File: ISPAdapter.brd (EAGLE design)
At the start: 63 x 34 mm, 3 parts

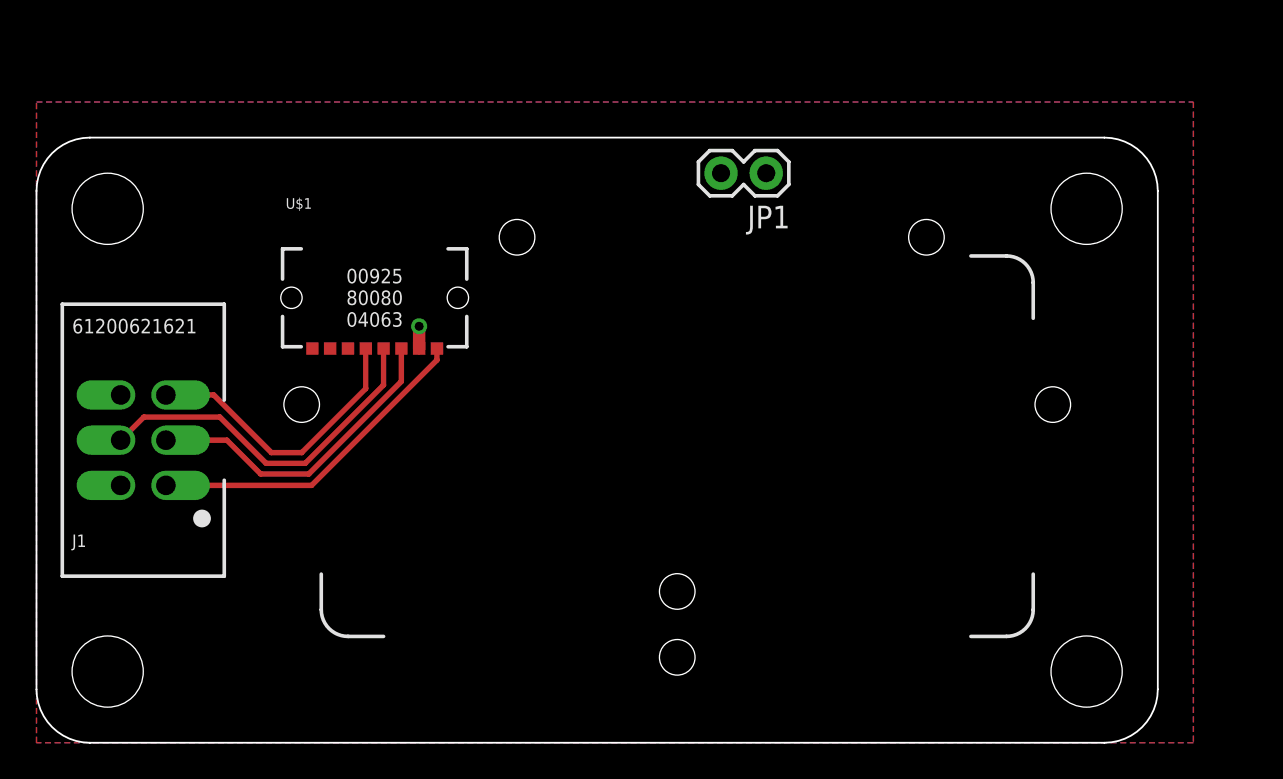
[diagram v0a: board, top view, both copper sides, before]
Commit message: Dropped ground layer
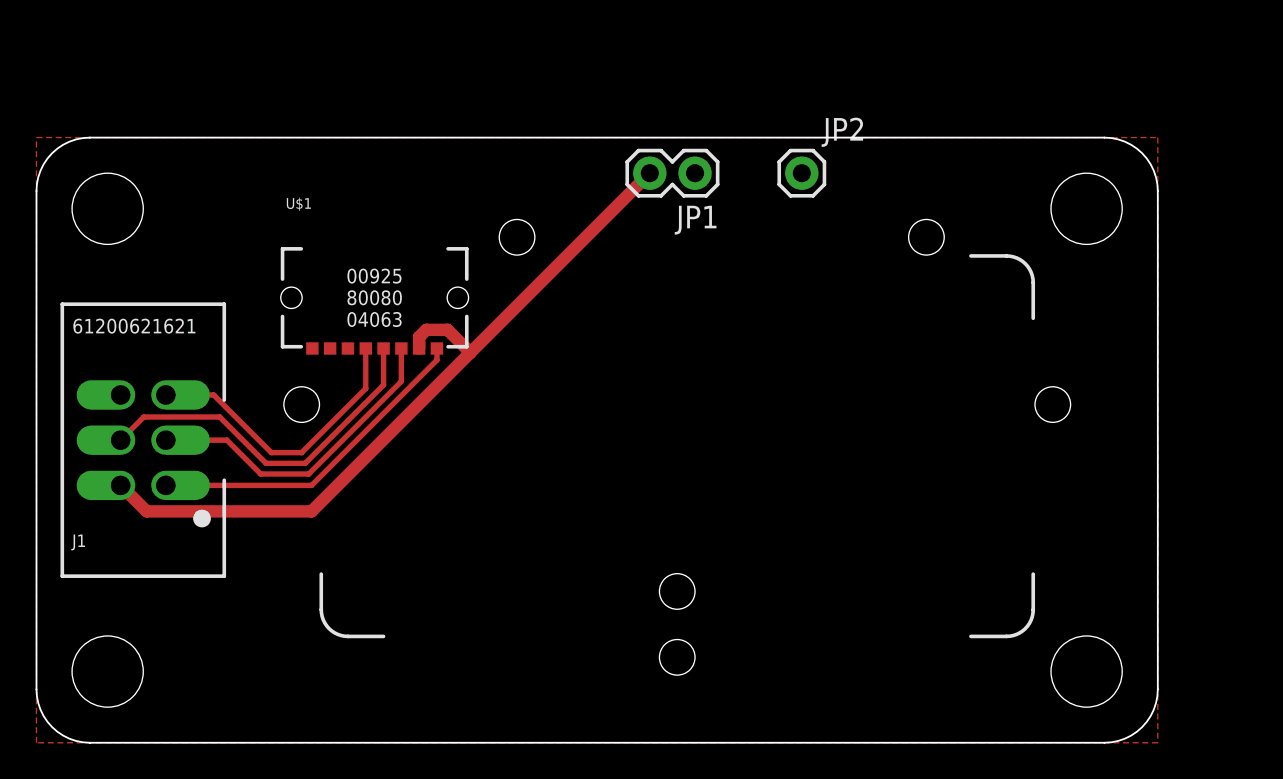
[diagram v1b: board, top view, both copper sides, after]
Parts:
- added JP2: M01PTH, SparkFun-Connectors:1X01
- moved JP1 4.00 mm to (37.0, 32.0)
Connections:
- net GND: now also JP2.1
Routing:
- net VCC: track 1.25 -> 42.4 mm, vias 1 -> 0
- removed copper zone on layer 16, net VCC
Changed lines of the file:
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@@
 <layer number="14" name="Route14" color="1" fill="6" visible="no" active="no"/>
 <layer number="15" name="Route15" color="4" fill="6" visible="no" active="no"/>
-<layer number="16" name="Bottom" color="1" fill="1" visible="no" active="yes"/>
+<layer number="16" name="Bottom" color="1" fill="1" visible="yes" active="yes"/>
 <layer number="17" name="Pads" color="2" fill="1" visible="yes" active="yes"/>
 <layer number="18" name="Vias" color="2" fill="1" visible="yes" active="yes"/>
@@
 <hole x="57.1" y="19" drill="2"/>
 <hole x="14.9" y="19" drill="2"/>
-<text x="41" y="30.2" size="1" layer="107" font="vector" ratio="20" rot="SR270" align="center-left">GND</text>
+<text x="37" y="30.2" size="1" layer="107" font="vector" ratio="20" rot="SR270" align="center-left">GND</text>
 <circle x="4" y="30" radius="2.7" width="0.5" layer="107"/>
-<text x="38.5" y="30.2" size="1" layer="107" font="vector" ratio="20" rot="SR270" align="center-left">+5V</text>
+<text x="34.5" y="30.2" size="1" layer="107" font="vector" ratio="20" rot="SR270" align="center-left">+5V</text>
 <text x="26" y="9" size="1" layer="107" font="vector" ratio="20" rot="SR0">1 MISO</text>
 <text x="19" y="9" size="1" layer="107" font="vector" ratio="20" rot="SR0">2 VCC</text>
@@
 <circle x="36" y="4.8" radius="1.7" width="0.5" layer="107"/>
 <circle x="14.9" y="19" radius="1.7" width="0.5" layer="107"/>
+<text x="43" y="30.2" size="1" layer="107" font="vector" ratio="20" rot="SR270" align="center-left">GND</text>
 </plain>
 <attributes>
@@
 <attribute name="DIGIKEY_PART_#" value="732-5394-ND" x="6" y="17" size="1.778" layer="27" display="off"/>
 </element>
-<element name="JP1" library="SparkFun-Connectors" package="1X02" value="M02PTH" x="41" y="32" rot="R180"/>
+<element name="JP1" library="SparkFun-Connectors" package="1X02" value="M02PTH" x="37" y="32" rot="R180"/>
 <element name="U$1" library="dubec" package="AVX9258-8P" value="AVX9258" x="19" y="25">
 <attribute name="MANUFACTURER" value="AVX Corporation" x="19" y="25" size="1.778" layer="27" display="off"/>
@@
 <attribute name="DIGIKEY_PART_#" value="478-5495-1-ND" x="19" y="25" size="1.778" layer="27" display="off"/>
 </element>
+<element name="JP2" library="SparkFun-Connectors" package="1X01" value="M01PTH" x="43" y="32"/>
 </elements>
 <signals>
@@
 <contactref element="JP1" pad="2"/>
 <contactref element="U$1" pad="2"/>
-<polygon width="0.3048" layer="16">
-<vertex x="0" y="0"/>
-<vertex x="0" y="36"/>
-<vertex x="65" y="36"/>
-<vertex x="65" y="0"/>
-</polygon>
-<via x="21.5" y="23.4" extent="1-16" drill="0.5"/>
-<wire x1="21.5" y1="22.15" x2="21.5" y2="23.4" width="0.7" layer="1"/>
+<wire x1="34.46" y1="32" x2="24.38" y2="21.92" width="0.7" layer="1"/>
+<wire x1="24.38" y1="21.92" x2="15.46" y2="13" width="0.7" layer="1"/>
+<wire x1="15.46" y1="13" x2="6.19" y2="13" width="0.7" layer="1"/>
+<wire x1="6.19" y1="13" x2="4.73" y2="14.46" width="0.7" layer="1"/>
+<wire x1="21.5" y1="22.15" x2="21.5" y2="22.8" width="0.7" layer="1"/>
+<wire x1="21.5" y1="22.8" x2="21.9" y2="23.2" width="0.7" layer="1"/>
+<wire x1="21.9" y1="23.2" x2="23.1" y2="23.2" width="0.7" layer="1"/>
+<wire x1="23.1" y1="23.2" x2="24.38" y2="21.92" width="0.7" layer="1"/>
 </signal>
 <signal name="MOSI">
@@
 <polygon width="0.3556" layer="1">
 <vertex x="0" y="0"/>
-<vertex x="0" y="36"/>
-<vertex x="65" y="36"/>
-<vertex x="65" y="0"/>
+<vertex x="0" y="34"/>
+<vertex x="63" y="34"/>
+<vertex x="63" y="0"/>
 </polygon>
 <contactref element="U$1" pad="8"/>
 <contactref element="U$1" pad="7"/>
 <contactref element="U$1" pad="6"/>
+<contactref element="JP2" pad="1"/>
 </signal>
 <signal name="MISO">

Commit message: Grounded screw holes; disconnected unused connector pins
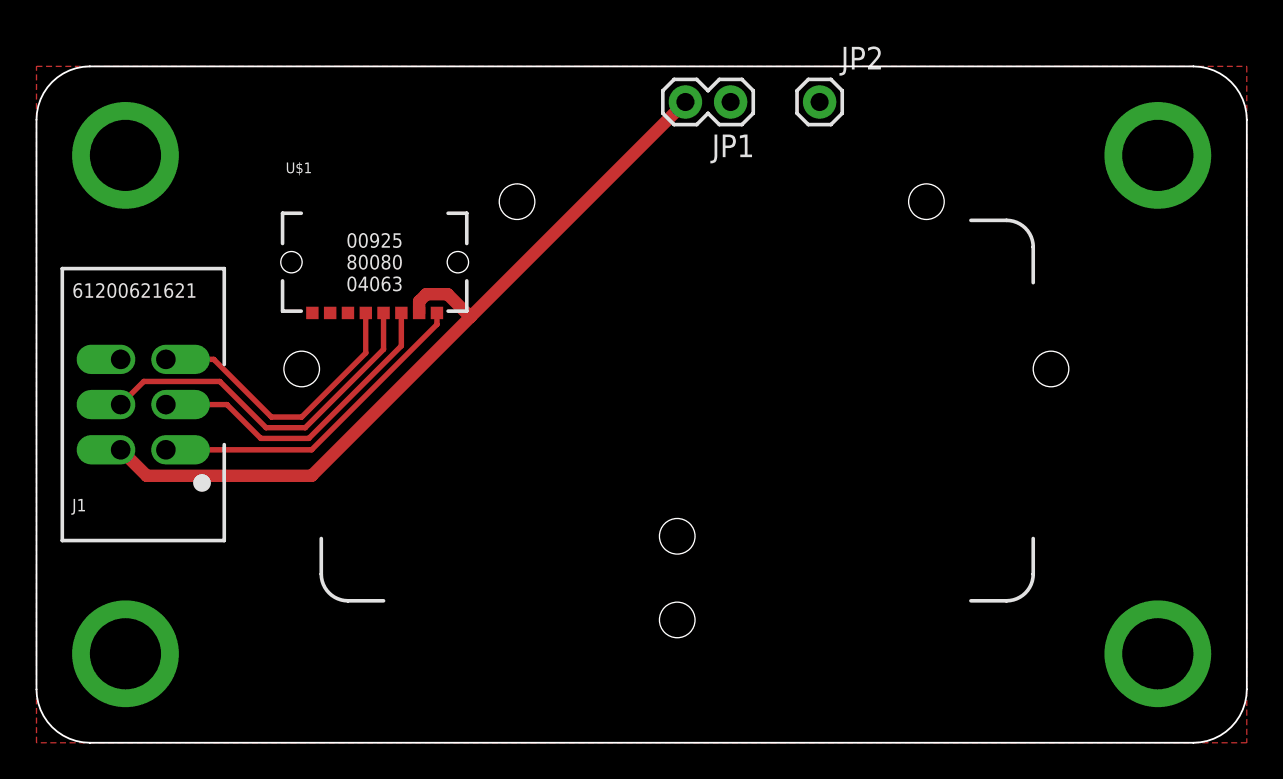
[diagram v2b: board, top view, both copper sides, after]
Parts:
- moved JP1 4.47 mm to (39.0, 36.0)
- moved JP2 4.12 mm to (44.0, 36.0)
- moved J1 2.00 mm to (6.00, 19.0)
- moved U$1 2.00 mm to (19.0, 27.0)
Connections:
- net GND: no longer U$1.7, U$1.8
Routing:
- net VCC: track 42.4 -> 45.3 mm
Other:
- board size 63 x 34 mm -> 68 x 38 mm

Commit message: Kelvin join?
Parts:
- moved JP2 9.70 mm to (34.3, 36.0)
- moved JP1 2.70 mm to (41.7, 36.0), turned to 0 degrees
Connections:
- new net DGND: J1.6, JP1.1, U$1.6
- net GND: no longer J1.6, JP1.1, U$1.6
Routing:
- net DGND: track 0.00 -> 44.0 mm
- net VCC: track 45.3 -> 53.0 mm
- net GND: track 0.00 -> 1.41 mm
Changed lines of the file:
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@@
 <hole x="57" y="21" drill="2"/>
 <hole x="14.9" y="21" drill="2"/>
-<text x="39.1" y="34.2" size="1" layer="107" font="vector" ratio="20" rot="SR270" align="center-left">GND</text>
-<text x="36.5" y="34.2" size="1" layer="107" font="vector" ratio="20" rot="SR270" align="center-left">+5V</text>
+<text x="41.7" y="34" size="1" layer="107" font="vector" ratio="20" rot="SR270" align="center-left">GND</text>
+<text x="44.3" y="34" size="1" layer="107" font="vector" ratio="20" rot="SR270" align="center-left">+5V</text>
 <text x="26" y="11" size="1" layer="107" font="vector" ratio="20" rot="SR0">1 MISO</text>
 <text x="19" y="11" size="1" layer="107" font="vector" ratio="20" rot="SR0">2 VCC</text>
@@
 <circle x="36" y="6.9" radius="1.7" width="0.5" layer="107"/>
 <circle x="14.9" y="21" radius="1.7" width="0.5" layer="107"/>
-<text x="44.1" y="34.2" size="1" layer="107" font="vector" ratio="20" rot="SR270" align="center-left">GND</text>
+<text x="34.3" y="34" size="1" layer="107" font="vector" ratio="20" rot="SR270" align="center-left">GND</text>
 </plain>
 <attributes>
@@
 <attribute name="DIGIKEY_PART_#" value="732-5394-ND" x="6" y="19" size="1.778" layer="27" display="off"/>
 </element>
-<element name="JP1" library="SparkFun-Connectors" package="1X02" value="M02PTH" x="39" y="36" rot="R180"/>
+<element name="JP1" library="SparkFun-Connectors" package="1X02" value="M02PTH" x="41.7" y="36"/>
 <element name="U$1" library="dubec" package="AVX9258-8P" value="AVX9258" x="19" y="27">
 <attribute name="MANUFACTURER" value="AVX Corporation" x="19" y="27" size="1.778" layer="27" display="off"/>
@@
 <attribute name="DIGIKEY_PART_#" value="478-5495-1-ND" x="19" y="27" size="1.778" layer="27" display="off"/>
 </element>
-<element name="JP2" library="SparkFun-Connectors" package="1X01" value="M01PTH" x="44" y="36"/>
+<element name="JP2" library="SparkFun-Connectors" package="1X01" value="M01PTH" x="34.3" y="36"/>
 </elements>
 <signals>
@@
 <contactref element="JP1" pad="2"/>
 <contactref element="U$1" pad="2"/>
-<wire x1="36.46" y1="36" x2="24.38" y2="23.92" width="0.7" layer="1"/>
+<wire x1="44.24" y1="36" x2="32.16" y2="23.92" width="0.7" layer="1"/>
 <wire x1="24.38" y1="23.92" x2="15.46" y2="15" width="0.7" layer="1"/>
 <wire x1="15.46" y1="15" x2="6.19" y2="15" width="0.7" layer="1"/>
@@
 <wire x1="21.9" y1="25.2" x2="23.1" y2="25.2" width="0.7" layer="1"/>
 <wire x1="23.1" y1="25.2" x2="24.38" y2="23.92" width="0.7" layer="1"/>
+<wire x1="32.16" y1="23.92" x2="24.38" y2="23.92" width="0.7" layer="1"/>
 </signal>
 <signal name="MOSI">
@@
 <wire x1="6.03" y1="20.3" x2="4.73" y2="19" width="0.3048" layer="1"/>
 </signal>
-<signal name="GND">
+<signal name="DGND">
 <contactref element="J1" pad="6"/>
 <contactref element="JP1" pad="1"/>
-<polygon width="0.3556" layer="1">
-<vertex x="0" y="0"/>
-<vertex x="0" y="38"/>
-<vertex x="68" y="38"/>
-<vertex x="68" y="0"/>
-</polygon>
-<contactref element="JP2" pad="1"/>
 <contactref element="U$1" pad="6"/>
-<via x="5" y="33" extent="1-16" drill="4"/>
-<via x="5" y="5" extent="1-16" drill="4"/>
-<via x="63" y="5" extent="1-16" drill="4"/>
-<via x="63" y="33" extent="1-16" drill="4"/>
+<wire x1="41.7" y1="36" x2="34.2" y2="28.5" width="0.7" layer="1"/>
+<wire x1="34.2" y1="28.5" x2="20.9" y2="28.5" width="0.7" layer="1"/>
+<wire x1="20.9" y1="28.5" x2="17.5" y2="25.1" width="0.7" layer="1"/>
+<wire x1="17.5" y1="25.1" x2="17.5" y2="24.15" width="0.7" layer="1"/>
+<wire x1="4.73" y1="21.54" x2="6.19" y2="23" width="0.7" layer="1"/>
+<wire x1="6.19" y1="23" x2="17.1" y2="23" width="0.7" layer="1"/>
+<wire x1="17.1" y1="23" x2="17.5" y2="23.4" width="0.7" layer="1"/>
+<wire x1="17.5" y1="23.4" x2="17.5" y2="24.15" width="0.7" layer="1"/>
 </signal>
 <signal name="MISO">
@@
 <wire x1="9.96" y1="21.54" x2="7.27" y2="21.54" width="0.3048" layer="1"/>
 </signal>
+<signal name="GND">
+<polygon width="0.3556" layer="1">
+<vertex x="0" y="0"/>
+<vertex x="0" y="38"/>
+<vertex x="68" y="38"/>
+<vertex x="68" y="0"/>
+</polygon>
+<via x="4" y="34" extent="1-16" drill="3.1"/>
+<via x="4" y="4" extent="1-16" drill="3.1"/>
+<via x="64" y="34" extent="1-16" drill="3.1"/>
+<via x="64" y="4" extent="1-16" drill="3.1"/>
+<contactref element="JP2" pad="1"/>
+<wire x1="40.7" y1="37" x2="41.7" y2="36" width="0.3048" layer="1"/>
+</signal>
 </signals>
+<errors>
+</errors>
 </board>
 </drawing>

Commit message: Tidying
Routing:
- net RESET: track 16.3 -> 15.4 mm
- net SCK: track 18.0 -> 17.1 mm
- net MOSI: track 20.3 -> 19.3 mm
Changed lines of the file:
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@@
 <hole x="50" y="30.4" drill="2"/>
 <hole x="57" y="21" drill="2"/>
-<hole x="14.9" y="21" drill="2"/>
+<hole x="15" y="21" drill="2"/>
 <text x="41.7" y="34" size="1" layer="107" font="vector" ratio="20" rot="SR270" align="center-left">GND</text>
 <text x="44.3" y="34" size="1" layer="107" font="vector" ratio="20" rot="SR270" align="center-left">+5V</text>
@@
 for Super DUBEC.
 Rev. 1</text>
-<text x="10" y="3" size="1" layer="107" font="vector" ratio="20" align="top-left">http://TURBOFUNCTION.com/fpv</text>
+<text x="4" y="3.5" size="1" layer="107" font="vector" ratio="20" align="top-left">http://TURBOFUNCTION.com/fpv</text>
 <text x="18" y="18" size="1" layer="107" font="vector" ratio="20">ISP connector pins:</text>
 <hole x="36" y="6.9" drill="2"/>
@@
 <circle x="36" y="11.6" radius="1.7" width="0.5" layer="107"/>
 <circle x="36" y="6.9" radius="1.7" width="0.5" layer="107"/>
-<circle x="14.9" y="21" radius="1.7" width="0.5" layer="107"/>
+<circle x="15" y="21" radius="1.7" width="0.5" layer="107"/>
 <text x="34.3" y="34" size="1" layer="107" font="vector" ratio="20" rot="SR270" align="center-left">GND</text>
 </plain>
@@
 <contactref element="JP1" pad="2"/>
 <contactref element="U$1" pad="2"/>
-<wire x1="44.24" y1="36" x2="32.16" y2="23.92" width="0.7" layer="1"/>
-<wire x1="24.38" y1="23.92" x2="15.46" y2="15" width="0.7" layer="1"/>
-<wire x1="15.46" y1="15" x2="6.19" y2="15" width="0.7" layer="1"/>
+<wire x1="44.24" y1="36" x2="35.66" y2="27.42" width="0.7" layer="1"/>
+<wire x1="16.76" y1="16.7" x2="11.3" y2="16.7" width="0.7" layer="1"/>
+<wire x1="11.3" y1="16.7" x2="9.6" y2="15" width="0.7" layer="1"/>
+<wire x1="9.6" y1="15" x2="6.19" y2="15" width="0.7" layer="1"/>
 <wire x1="6.19" y1="15" x2="4.73" y2="16.46" width="0.7" layer="1"/>
 <wire x1="21.5" y1="24.15" x2="21.5" y2="24.8" width="0.7" layer="1"/>
-<wire x1="21.5" y1="24.8" x2="21.9" y2="25.2" width="0.7" layer="1"/>
-<wire x1="21.9" y1="25.2" x2="23.1" y2="25.2" width="0.7" layer="1"/>
-<wire x1="23.1" y1="25.2" x2="24.38" y2="23.92" width="0.7" layer="1"/>
-<wire x1="32.16" y1="23.92" x2="24.38" y2="23.92" width="0.7" layer="1"/>
+<wire x1="35.66" y1="27.42" x2="26.22" y2="27.42" width="0.7" layer="1"/>
+<wire x1="16.76" y1="16.7" x2="24" y2="23.94" width="0.7" layer="1"/>
+<wire x1="26.22" y1="27.42" x2="24" y2="25.2" width="0.7" layer="1"/>
+<wire x1="24" y1="25.2" x2="21.9" y2="25.2" width="0.7" layer="1"/>
+<wire x1="21.9" y1="25.2" x2="21.5" y2="24.8" width="0.7" layer="1"/>
+<wire x1="24" y1="23.94" x2="24" y2="25.2" width="0.7" layer="1"/>
 </signal>
 <signal name="MOSI">
 <contactref element="J1" pad="4"/>
 <contactref element="U$1" pad="4"/>
-<wire x1="19.5" y1="24.15" x2="19.5" y2="22.1" width="0.3048" layer="1"/>
-<wire x1="19.5" y1="22.1" x2="15.1" y2="17.7" width="0.3048" layer="1"/>
-<wire x1="15.1" y1="17.7" x2="12.9" y2="17.7" width="0.3048" layer="1"/>
-<wire x1="12.9" y1="17.7" x2="10.3" y2="20.3" width="0.3048" layer="1"/>
-<wire x1="10.3" y1="20.3" x2="6.03" y2="20.3" width="0.3048" layer="1"/>
+<wire x1="19.5" y1="24.15" x2="19.5" y2="22.3" width="0.3048" layer="1"/>
+<wire x1="19.5" y1="22.3" x2="15.9" y2="18.7" width="0.3048" layer="1"/>
+<wire x1="15.9" y1="18.7" x2="11.1" y2="18.7" width="0.3048" layer="1"/>
+<wire x1="11.1" y1="18.7" x2="9.5" y2="20.3" width="0.3048" layer="1"/>
+<wire x1="9.5" y1="20.3" x2="6.03" y2="20.3" width="0.3048" layer="1"/>
 <wire x1="6.03" y1="20.3" x2="4.73" y2="19" width="0.3048" layer="1"/>
 </signal>
@@
 <contactref element="JP1" pad="1"/>
 <contactref element="U$1" pad="6"/>
-<wire x1="41.7" y1="36" x2="34.2" y2="28.5" width="0.7" layer="1"/>
-<wire x1="34.2" y1="28.5" x2="20.9" y2="28.5" width="0.7" layer="1"/>
-<wire x1="20.9" y1="28.5" x2="17.5" y2="25.1" width="0.7" layer="1"/>
-<wire x1="17.5" y1="25.1" x2="17.5" y2="24.15" width="0.7" layer="1"/>
+<wire x1="35.3" y1="28.5" x2="23.1" y2="28.5" width="0.7" layer="1"/>
+<wire x1="23.1" y1="28.5" x2="19.8" y2="25.2" width="0.7" layer="1"/>
+<wire x1="19.8" y1="25.2" x2="17.9" y2="25.2" width="0.7" layer="1"/>
+<wire x1="17.9" y1="25.2" x2="17.5" y2="24.8" width="0.7" layer="1"/>
+<wire x1="17.5" y1="24.8" x2="17.5" y2="24.15" width="0.7" layer="1"/>
 <wire x1="4.73" y1="21.54" x2="6.19" y2="23" width="0.7" layer="1"/>
-<wire x1="6.19" y1="23" x2="17.1" y2="23" width="0.7" layer="1"/>
-<wire x1="17.1" y1="23" x2="17.5" y2="23.4" width="0.7" layer="1"/>
-<wire x1="17.5" y1="23.4" x2="17.5" y2="24.15" width="0.7" layer="1"/>
+<wire x1="6.19" y1="23" x2="17" y2="23" width="0.7" layer="1"/>
+<wire x1="17" y1="23" x2="17.5" y2="23.5" width="0.7" layer="1"/>
+<wire x1="17.5" y1="23.5" x2="17.5" y2="24.15" width="0.7" layer="1"/>
+<wire x1="35.3" y1="28.5" x2="41.7" y2="34.9" width="0.7" layer="1"/>
+<wire x1="41.7" y1="34.9" x2="41.7" y2="36" width="0.7" layer="1"/>
 </signal>
 <signal name="MISO">
 <contactref element="J1" pad="1"/>
 <contactref element="U$1" pad="1"/>
-<wire x1="22.5" y1="24.15" x2="22.5" y2="23.5" width="0.3048" layer="1"/>
-<wire x1="22.5" y1="23.5" x2="15.46" y2="16.46" width="0.3048" layer="1"/>
-<wire x1="15.46" y1="16.46" x2="7.27" y2="16.46" width="0.3048" layer="1"/>
+<wire x1="22.3" y1="23.5" x2="16.26" y2="17.46" width="0.3048" layer="1"/>
+<wire x1="16.26" y1="17.46" x2="10.96" y2="17.46" width="0.3048" layer="1"/>
+<wire x1="10.96" y1="17.46" x2="9.96" y2="16.46" width="0.3048" layer="1"/>
+<wire x1="9.96" y1="16.46" x2="7.27" y2="16.46" width="0.3048" layer="1"/>
+<wire x1="22.3" y1="23.5" x2="22.3" y2="23.95" width="0.3048" layer="1"/>
+<wire x1="22.3" y1="23.95" x2="22.5" y2="24.15" width="0.3048" layer="1"/>
 </signal>
 <signal name="SCK">
 <contactref element="J1" pad="3"/>
 <contactref element="U$1" pad="3"/>
-<wire x1="20.5" y1="24.15" x2="20.5" y2="22.3" width="0.3048" layer="1"/>
-<wire x1="20.5" y1="22.3" x2="15.3" y2="17.1" width="0.3048" layer="1"/>
-<wire x1="15.3" y1="17.1" x2="12.6" y2="17.1" width="0.3048" layer="1"/>
-<wire x1="12.6" y1="17.1" x2="10.7" y2="19" width="0.3048" layer="1"/>
-<wire x1="10.7" y1="19" x2="7.27" y2="19" width="0.3048" layer="1"/>
+<wire x1="20.5" y1="24.15" x2="20.5" y2="22.5" width="0.3048" layer="1"/>
+<wire x1="20.5" y1="22.5" x2="16.1" y2="18.1" width="0.3048" layer="1"/>
+<wire x1="16.1" y1="18.1" x2="10.9" y2="18.1" width="0.3048" layer="1"/>
+<wire x1="10.9" y1="18.1" x2="10" y2="19" width="0.3048" layer="1"/>
+<wire x1="10" y1="19" x2="7.27" y2="19" width="0.3048" layer="1"/>
 </signal>
 <signal name="RESET">
 <contactref element="J1" pad="5"/>
 <contactref element="U$1" pad="5"/>
-<wire x1="18.5" y1="24.15" x2="18.5" y2="21.9" width="0.3048" layer="1"/>
-<wire x1="18.5" y1="21.9" x2="14.9" y2="18.3" width="0.3048" layer="1"/>
-<wire x1="14.9" y1="18.3" x2="13.2" y2="18.3" width="0.3048" layer="1"/>
-<wire x1="13.2" y1="18.3" x2="9.96" y2="21.54" width="0.3048" layer="1"/>
-<wire x1="9.96" y1="21.54" x2="7.27" y2="21.54" width="0.3048" layer="1"/>
+<wire x1="18.5" y1="24.15" x2="18.5" y2="22.1" width="0.3048" layer="1"/>
+<wire x1="18.5" y1="22.1" x2="15.7" y2="19.3" width="0.3048" layer="1"/>
+<wire x1="15.7" y1="19.3" x2="11.4" y2="19.3" width="0.3048" layer="1"/>
+<wire x1="11.4" y1="19.3" x2="9.16" y2="21.54" width="0.3048" layer="1"/>
+<wire x1="9.16" y1="21.54" x2="7.27" y2="21.54" width="0.3048" layer="1"/>
 </signal>
 <signal name="GND">
@@
 <vertex x="68" y="0"/>
 </polygon>
-<via x="4" y="34" extent="1-16" drill="3.1"/>
-<via x="4" y="4" extent="1-16" drill="3.1"/>
-<via x="64" y="34" extent="1-16" drill="3.1"/>
-<via x="64" y="4" extent="1-16" drill="3.1"/>
+<via x="6" y="30" extent="1-16" drill="3.1"/>
+<via x="6" y="8" extent="1-16" drill="3.1"/>
+<via x="63" y="33" extent="1-16" drill="3.1"/>
+<via x="63" y="5" extent="1-16" drill="3.1"/>
 <contactref element="JP2" pad="1"/>
 <wire x1="40.7" y1="37" x2="41.7" y2="36" width="0.3048" layer="1"/>
